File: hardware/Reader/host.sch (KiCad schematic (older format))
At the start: 7 parts, among them IC1 NodeMCU_ESP32_DevKit

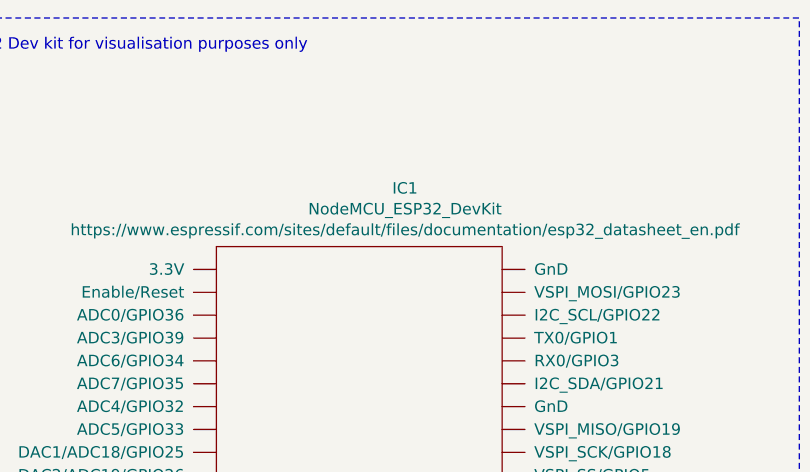
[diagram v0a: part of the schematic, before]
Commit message: Added ESD Protection. Fixed minor bugs on schematic. Attempted placement of components
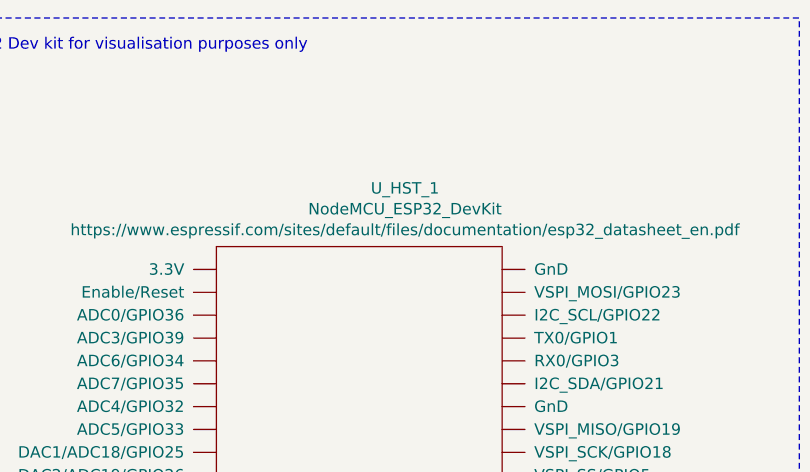
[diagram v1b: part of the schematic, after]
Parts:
- renumbered IC1 to U_HST_1
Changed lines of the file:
@@
 $Descr USLetter 11000 8500
 encoding utf-8
-Sheet 17 18
+Sheet 13 19
 Title "CANnect Reader | Host"
-Date "2020-10-20"
-Rev "0.0.01"
+Date "2020-10-25"
+Rev "0.0.03"
 Comp "CANtech"
 Comment1 "Created by Choong Jin Ng | jin8383@gmail.com"
@@
 P 5550 6500
 AR Path="/5F91DA68" Ref="IC?"  Part="1"
-AR Path="/5F91C7D3/5F91DA68" Ref="IC1"  Part="1"
-F 0 "IC1" H 5725 10105 50  0000 C CNN
+AR Path="/5F91C7D3/5F91DA68" Ref="U_HST_1"  Part="1"
+F 0 "U_HST_1" H 5725 10105 50  0000 C CNN
 F 1 "NodeMCU_ESP32_DevKit" H 5725 10014 50  0000 C CNN
 F 2 "" H 5550 6500 50  0001 C CNN

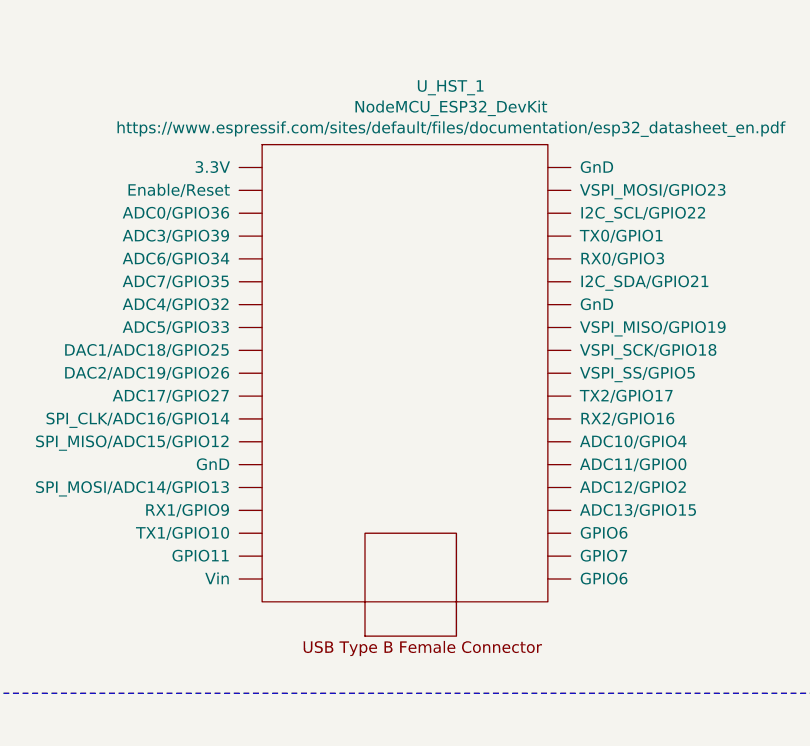
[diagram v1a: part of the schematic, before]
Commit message: Fixed bugs on the reader schematic. Exported Schematic Electrical report
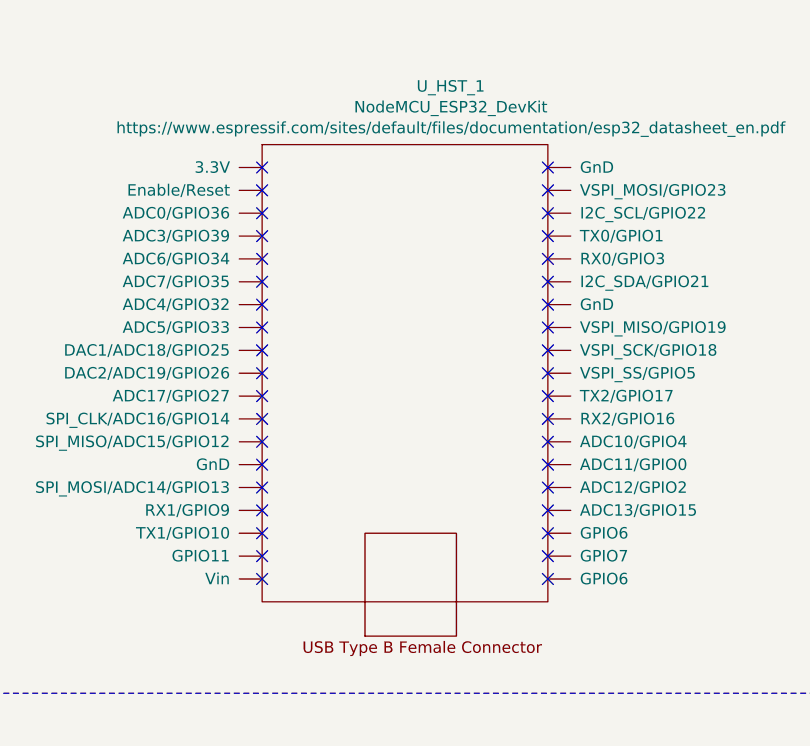
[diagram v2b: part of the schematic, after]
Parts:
- J_HST_1, J_HST_2, J_HST_3, J_HST_4, J_HST_5, J_HST_6: Manufacturer (none) -> TE Connectivity AMP Connectors; Vendor (none) -> DigiKey Canada; digikeypn (none) -> A113314-ND
- U_HST_1: Part Name (none) -> NodeMCU_ESP32_DevKit; Vendor (none) -> Amazon Canada
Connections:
- no-connect marks 14 -> 52
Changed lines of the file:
@@
 F 3 "" H 5550 6500 50  0001 C CNN
 F 4 "https://www.espressif.com/sites/default/files/documentation/esp32_datasheet_en.pdf" H 5725 9923 50  0000 C CNN "Website"
+F 5 "NodeMCU_ESP32_DevKit" H 5550 6500 50  0001 C CNN "Part Name"
+F 6 "Amazon Canada" H 5550 6500 50  0001 C CNN "Vendor"
 	1    5550 6500
 	1    0    0    -1
@@
 F 3 "https://www.te.com/commerce/DocumentDelivery/DDEController?Action=srchrtrv&DocNm=282832&DocType=Customer+Drawing&DocLang=English" H 1950 3350 60  0001 C CNN
 F 4 "282832-2" H 1950 3350 50  0001 C CNN "Part Name"
+F 5 "DigiKey Canada" H 1950 3350 50  0001 C CNN "Vendor"
+F 6 "TE Connectivity AMP Connectors" H 1950 3350 50  0001 C CNN "Manufacturer"
+F 7 "A113314-ND" H 1950 3350 50  0001 C CNN "digikeypn"
 	1    1950 3350
 	0    -1   -1   0
@@
 F 3 "https://www.te.com/commerce/DocumentDelivery/DDEController?Action=srchrtrv&DocNm=282832&DocType=Customer+Drawing&DocLang=English" H 2800 3350 60  0001 C CNN
 F 4 "282832-2" H 2800 3350 50  0001 C CNN "Part Name"
+F 5 "DigiKey Canada" H 2800 3350 50  0001 C CNN "Vendor"
+F 6 "TE Connectivity AMP Connectors" H 2800 3350 50  0001 C CNN "Manufacturer"
+F 7 "A113314-ND" H 2800 3350 50  0001 C CNN "digikeypn"
 	1    2800 3350
 	0    -1   -1   0
@@
 F 3 "https://www.te.com/commerce/DocumentDelivery/DDEController?Action=srchrtrv&DocNm=282832&DocType=Customer+Drawing&DocLang=English" H 2450 5500 60  0001 C CNN
 F 4 "282832-2" H 2450 5500 50  0001 C CNN "Part Name"
+F 5 "DigiKey Canada" H 2450 5500 50  0001 C CNN "Vendor"
+F 6 "TE Connectivity AMP Connectors" H 2450 5500 50  0001 C CNN "Manufacturer"
+F 7 "A113314-ND" H 2450 5500 50  0001 C CNN "digikeypn"
 	1    2450 5500
 	0    1    1    0
@@
 F 3 "https://www.te.com/commerce/DocumentDelivery/DDEController?Action=srchrtrv&DocNm=282832&DocType=Customer+Drawing&DocLang=English" H 8350 2900 60  0001 C CNN
 F 4 "282832-2" H 8350 2900 50  0001 C CNN "Part Name"
+F 5 "DigiKey Canada" H 8350 2900 50  0001 C CNN "Vendor"
+F 6 "TE Connectivity AMP Connectors" H 8350 2900 50  0001 C CNN "Manufacturer"
+F 7 "A113314-ND" H 8350 2900 50  0001 C CNN "digikeypn"
 	1    8350 2900
 	0    -1   -1   0
@@
 F 3 "https://www.te.com/commerce/DocumentDelivery/DDEController?Action=srchrtrv&DocNm=282832&DocType=Customer+Drawing&DocLang=English" H 9250 2900 60  0001 C CNN
 F 4 "282832-2" H 9250 2900 50  0001 C CNN "Part Name"
+F 5 "DigiKey Canada" H 9250 2900 50  0001 C CNN "Vendor"
+F 6 "TE Connectivity AMP Connectors" H 9250 2900 50  0001 C CNN "Manufacturer"
+F 7 "A113314-ND" H 9250 2900 50  0001 C CNN "digikeypn"
 	1    9250 2900
 	0    -1   -1   0
@@
 F 3 "https://www.te.com/commerce/DocumentDelivery/DDEController?Action=srchrtrv&DocNm=282832&DocType=Customer+Drawing&DocLang=English" H 8850 4550 60  0001 C CNN
 F 4 "282832-2" H 8850 4550 50  0001 C CNN "Part Name"
+F 5 "DigiKey Canada" H 8850 4550 50  0001 C CNN "Vendor"
+F 6 "TE Connectivity AMP Connectors" H 8850 4550 50  0001 C CNN "Manufacturer"
+F 7 "A113314-ND" H 8850 4550 50  0001 C CNN "digikeypn"
 	1    8850 4550
 	0    1    1    0
@@
 Wire Wire Line
 	9600 4350 9600 5400
+NoConn ~ 4900 3250
+NoConn ~ 4900 3350
+NoConn ~ 4900 3450
+NoConn ~ 4900 3550
+NoConn ~ 4900 3650
+NoConn ~ 4900 3750
+NoConn ~ 4900 3850
+NoConn ~ 4900 3950
+NoConn ~ 4900 4050
+NoConn ~ 4900 4150
+NoConn ~ 4900 4250
+NoConn ~ 4900 4350
+NoConn ~ 4900 4450
+NoConn ~ 4900 4550
+NoConn ~ 4900 4650
+NoConn ~ 4900 4750
+NoConn ~ 4900 4850
+NoConn ~ 4900 4950
+NoConn ~ 4900 5050
+NoConn ~ 6150 5050
+NoConn ~ 6150 4950
+NoConn ~ 6150 4850
+NoConn ~ 6150 4750
+NoConn ~ 6150 4650
+NoConn ~ 6150 4550
+NoConn ~ 6150 4450
+NoConn ~ 6150 4350
+NoConn ~ 6150 4250
+NoConn ~ 6150 4150
+NoConn ~ 6150 4050
+NoConn ~ 6150 3950
+NoConn ~ 6150 3850
+NoConn ~ 6150 3750
+NoConn ~ 6150 3650
+NoConn ~ 6150 3550
+NoConn ~ 6150 3450
+NoConn ~ 6150 3350
+NoConn ~ 6150 3250
 $EndSCHEMATC

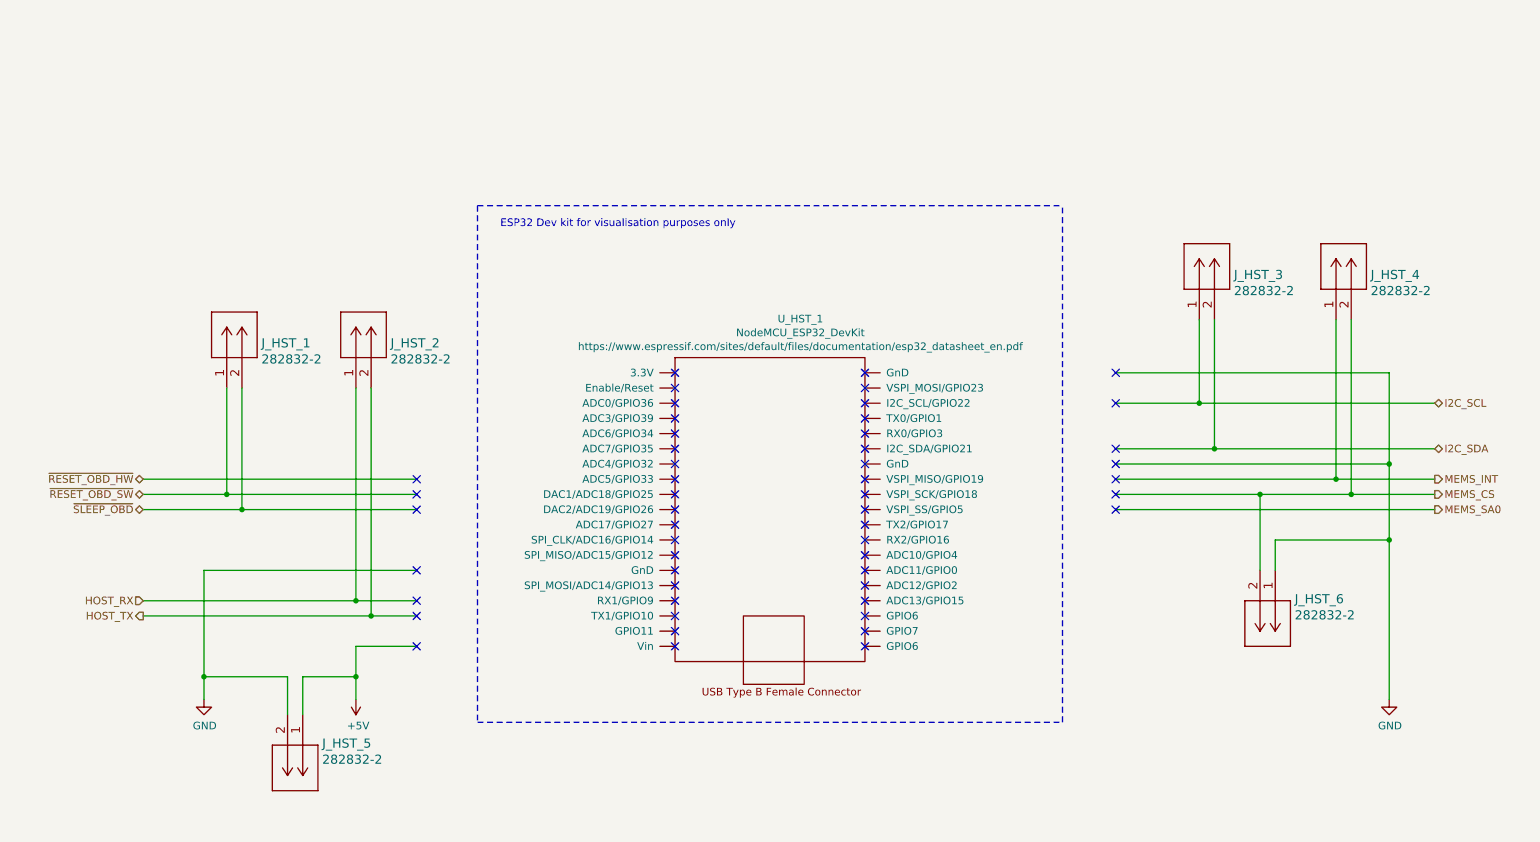
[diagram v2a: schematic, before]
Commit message: Fixed wiring issue on ESD Protection
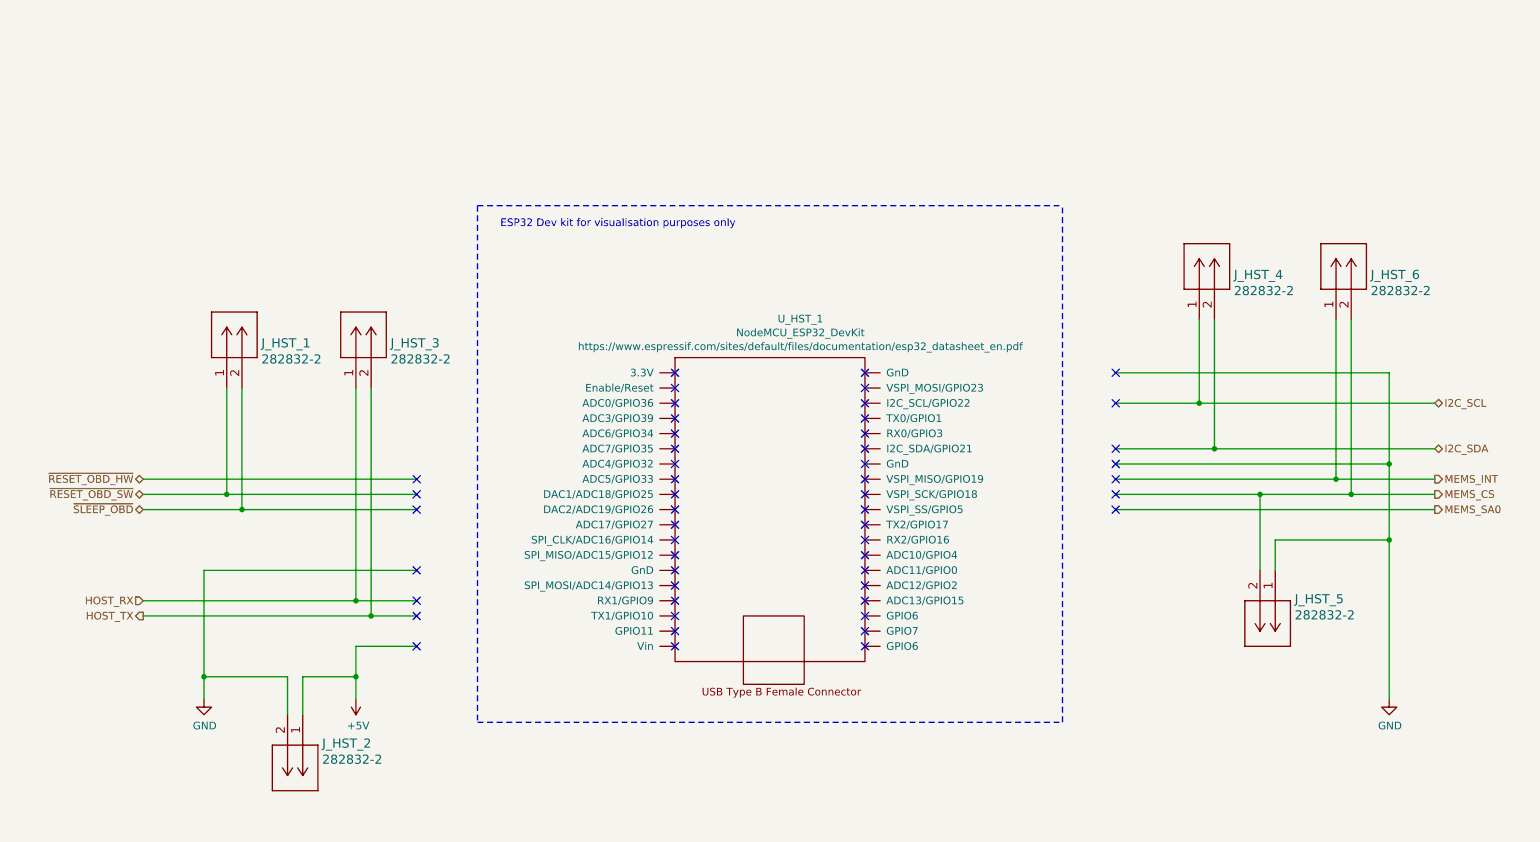
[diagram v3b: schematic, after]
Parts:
- renumbered J_HST_5 to J_HST_2, J_HST_2 to J_HST_3, J_HST_3 to J_HST_4, J_HST_6 to J_HST_5, J_HST_4 to J_HST_6
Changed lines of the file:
@@
 	7800 3450 8350 3450
 $Comp
-L power:GND #PWR05
+L power:GND #PWR086
 U 1 1 5F91E2ED
 P 9600 5400
-F 0 "#PWR05" H 9600 5150 50  0001 C CNN
+F 0 "#PWR086" H 9600 5150 50  0001 C CNN
 F 1 "GND" H 9605 5227 50  0000 C CNN
 F 2 "" H 9600 5400 50  0001 C CNN
@@
 	1400 4150 2050 4150
 $Comp
-L power:GND #PWR03
+L power:GND #PWR084
 U 1 1 5F91E8F3
 P 1800 5400
-F 0 "#PWR03" H 1800 5150 50  0001 C CNN
+F 0 "#PWR084" H 1800 5150 50  0001 C CNN
 F 1 "GND" H 1805 5227 50  0000 C CNN
 F 2 "" H 1800 5400 50  0001 C CNN
@@
 	1800 5400 1800 5250
 $Comp
-L power:+5V #PWR04
+L power:+5V #PWR085
 U 1 1 5F91DA5E
 P 2800 5400
-F 0 "#PWR04" H 2800 5250 50  0001 C CNN
+F 0 "#PWR085" H 2800 5250 50  0001 C CNN
 F 1 "+5V" H 2815 5573 50  0000 C CNN
 F 2 "" H 2800 5400 50  0001 C CNN
@@
 	2800 5400 2800 5250
 $Comp
-L CANtech:NodeMCU_ESP32_DevKit IC?
+L CANtech:NodeMCU_ESP32_DevKit U_HST_?
 U 1 1 5F91DA68
 P 5550 6500
-AR Path="/5F91DA68" Ref="IC?"  Part="1"
+AR Path="/5F91DA68" Ref="U_HST_?"  Part="1"
 AR Path="/5F91C7D3/5F91DA68" Ref="U_HST_1"  Part="1"
 F 0 "U_HST_1" H 5725 10105 50  0000 C CNN
@@
 $EndComp
 $Comp
-L 2828322:282832-2 J_HST_2
+L 2828322:282832-2 J_HST_3
 U 1 1 5F9D9258
 P 2800 3350
-F 0 "J_HST_2" V 3095 3122 60  0000 R CNN
+F 0 "J_HST_3" V 3095 3122 60  0000 R CNN
 F 1 "282832-2" V 2989 3122 60  0000 R CNN
 F 2 "footprints:282832-2" H 3200 3290 60  0001 C CNN
@@
 $EndComp
 $Comp
-L 2828322:282832-2 J_HST_5
+L 2828322:282832-2 J_HST_2
 U 1 1 5F9D9519
 P 2450 5500
-F 0 "J_HST_5" V 2639 5628 60  0000 L CNN
+F 0 "J_HST_2" V 2639 5628 60  0000 L CNN
 F 1 "282832-2" V 2745 5628 60  0000 L CNN
 F 2 "footprints:282832-2" H 2850 5440 60  0001 C CNN
@@
 $EndComp
 $Comp
-L 2828322:282832-2 J_HST_3
+L 2828322:282832-2 J_HST_4
 U 1 1 5F9DA91B
 P 8350 2900
-F 0 "J_HST_3" V 8645 2672 60  0000 R CNN
+F 0 "J_HST_4" V 8645 2672 60  0000 R CNN
 F 1 "282832-2" V 8539 2672 60  0000 R CNN
 F 2 "footprints:282832-2" H 8750 2840 60  0001 C CNN
@@
 $EndComp
 $Comp
-L 2828322:282832-2 J_HST_4
+L 2828322:282832-2 J_HST_6
 U 1 1 5F9DB09C
 P 9250 2900
-F 0 "J_HST_4" V 9545 2672 60  0000 R CNN
+F 0 "J_HST_6" V 9545 2672 60  0000 R CNN
 F 1 "282832-2" V 9439 2672 60  0000 R CNN
 F 2 "footprints:282832-2" H 9650 2840 60  0001 C CNN
@@
 	7800 4150 9900 4150
 $Comp
-L 2828322:282832-2 J_HST_6
+L 2828322:282832-2 J_HST_5
 U 1 1 5F9F4BEC
 P 8850 4550
-F 0 "J_HST_6" V 9039 4678 60  0000 L CNN
+F 0 "J_HST_5" V 9039 4678 60  0000 L CNN
 F 1 "282832-2" V 9145 4678 60  0000 L CNN
 F 2 "footprints:282832-2" H 9250 4490 60  0001 C CNN
